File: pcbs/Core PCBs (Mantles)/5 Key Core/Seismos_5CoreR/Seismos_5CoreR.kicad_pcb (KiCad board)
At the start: 2 copper layers, 147 x 78 mm, 27 parts, among them J1 SM09B-SRSS-TB(LF)(SN), J2 SM09B-SRSS-TB(LF)(SN), J3 SM09B-SRSS-TB(LF)(SN), J4 SM09B-SRSS-TB(LF)(SN), J5 SM09B-SRSS-TB(LF)(SN), J6 SM09B-SRSS-TB(LF)(SN), J7 SM09B-SRSS-TB(LF)(SN), J8 MJ-4PP-9-Lily58, J9 Conn_01x05_Pin, SW1 RotaryEncoder_Switch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

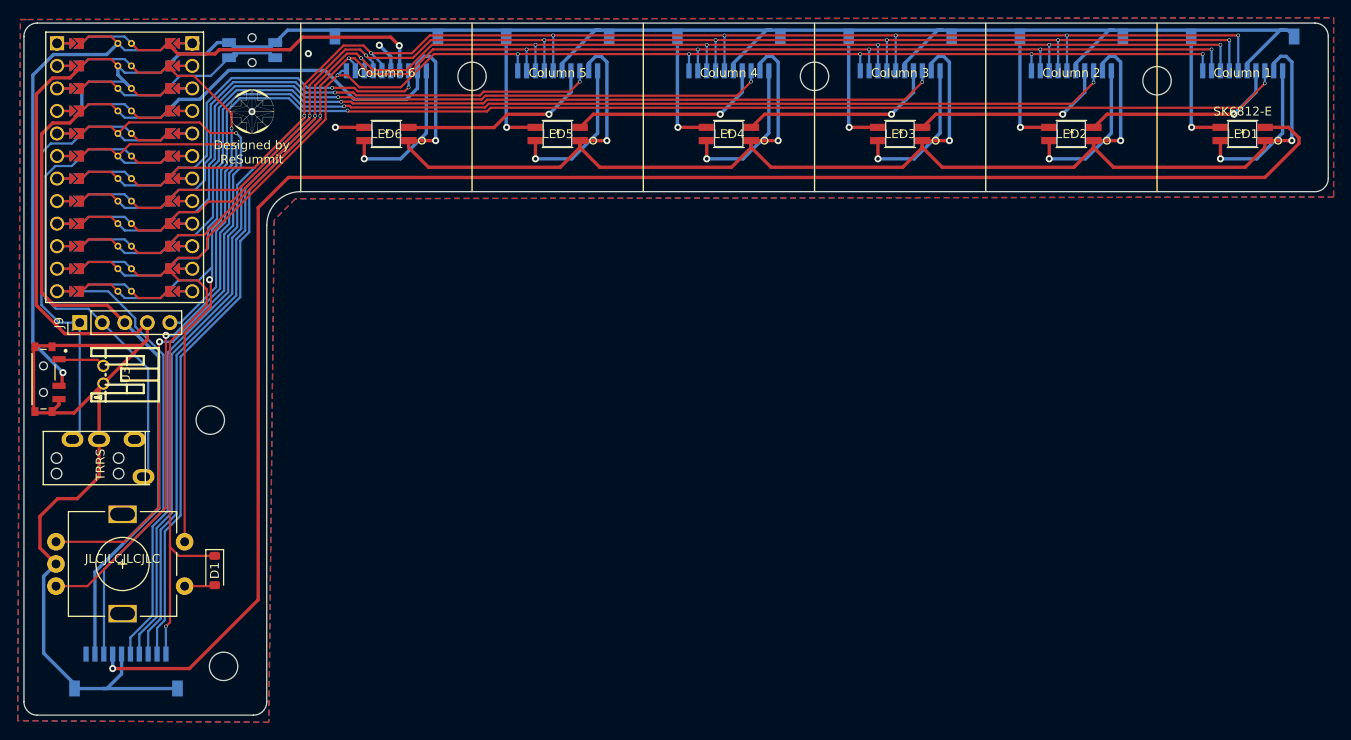
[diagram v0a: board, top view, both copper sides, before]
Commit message: Release v1.1
***NOTE***: If you have a previous commit, please update your files.
This commit fixes the incorrect RGB pinout and power switch as the
RGB footprint was incorrect.
The power switch behaviour is also fixed in this commit so the position
matches on both sides.
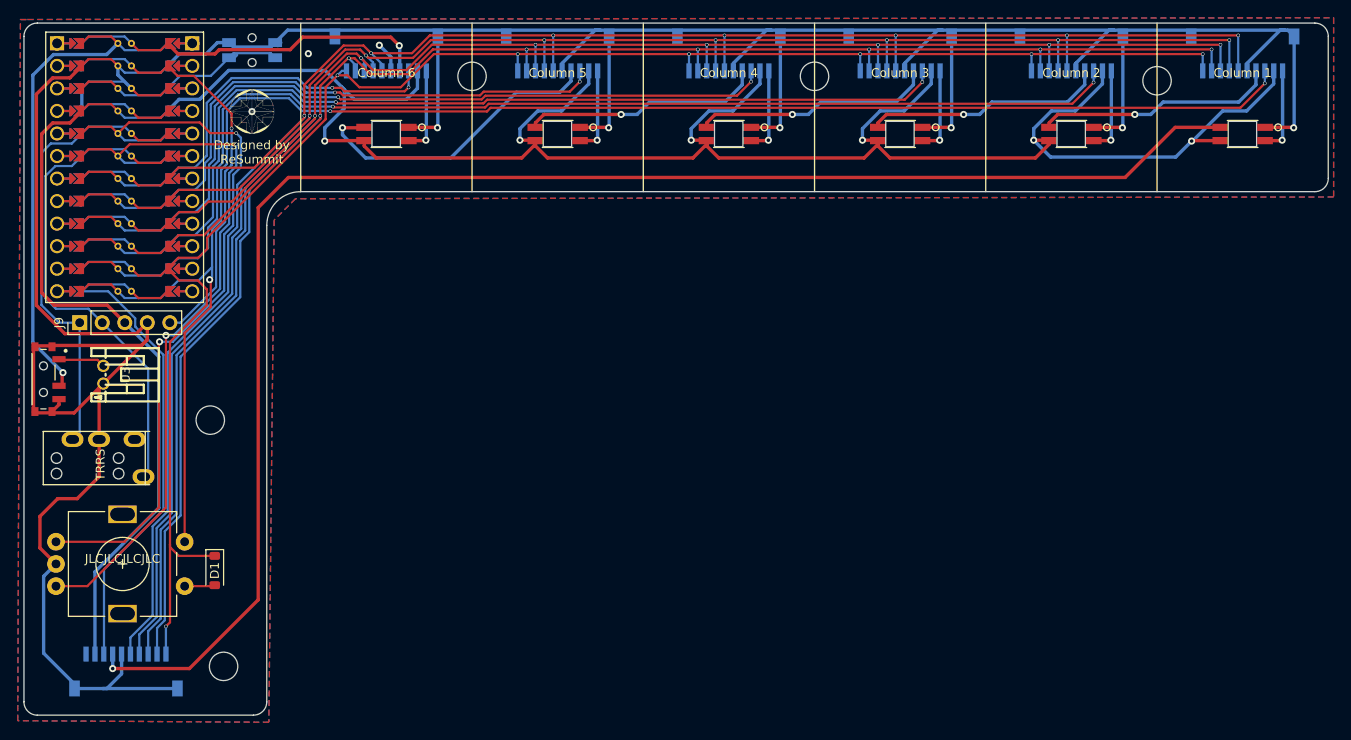
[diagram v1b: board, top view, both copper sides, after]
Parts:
- LED1, LED2, LED3, LED4, LED5, LED6: moved to F.Cu
- turned LED1 to 180 degrees
- turned LED2 to 180 degrees
- turned LED3 to 180 degrees
- turned LED4 to 180 degrees
- turned LED5 to 180 degrees
- turned LED6 to 180 degrees
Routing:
- net /V+: track 315.9 -> 301.2 mm
- net /RGB_In7: track 190.7 -> 177.6 mm
- net /RGB_In2: track 22.3 -> 34.8 mm
- net GND: track 385.6 -> 396.2 mm
- net /RGB_Out6: track 17.3 -> 9.80 mm
- net /RGB_Out4: track 17.3 -> 9.80 mm
- net /RGB_Out1: track 17.3 -> 9.80 mm
- net /RGB_Out3: track 17.3 -> 9.80 mm
- net /RGB_Out2: track 17.3 -> 9.80 mm
- net /RGB_Out5: track 17.3 -> 9.80 mm
- net /RGB_In4: track 22.3 -> 27.1 mm
- net /RGB_In6: track 22.3 -> 27.1 mm
- net /RGB_In3: track 22.3 -> 27.1 mm
- net /RGB_In5: track 22.3 -> 27.1 mm
- net SDA: track 42.4 -> 41.2 mm
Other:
- board text added: "Rev. 1.1"
- board text removed: "Rev. 1.0"

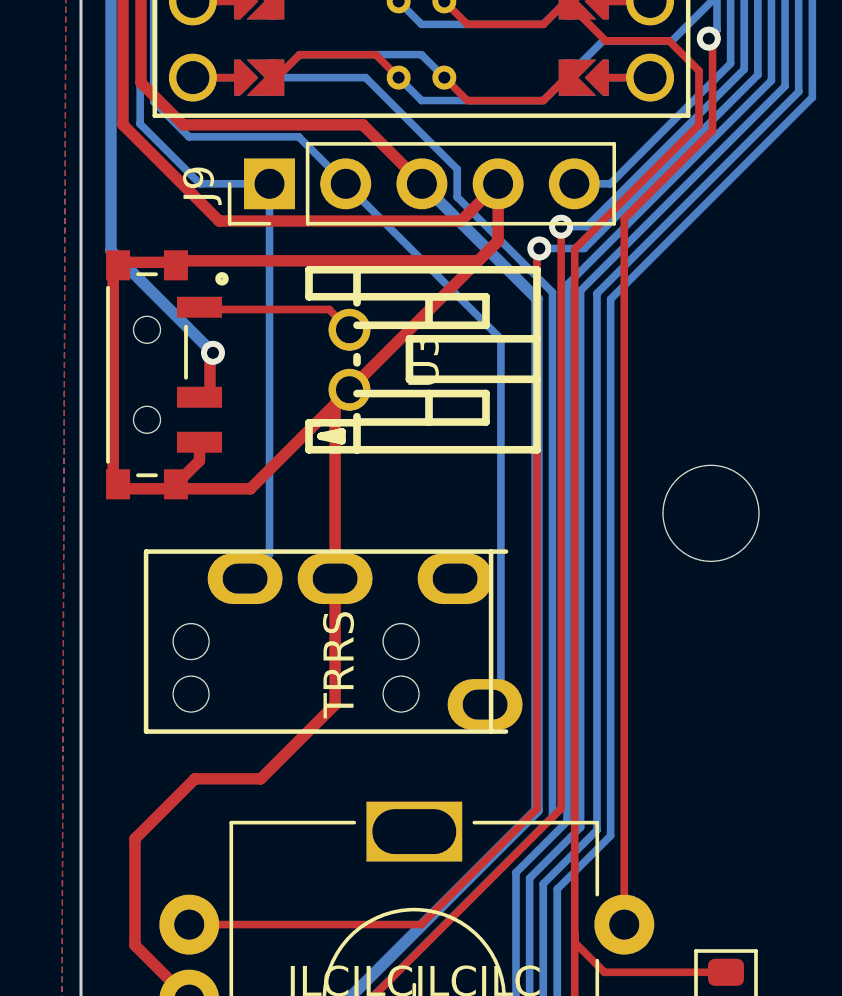
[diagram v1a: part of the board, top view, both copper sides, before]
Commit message: Release v1.1.1
Added I2C pull up resistors and bridge contacts on the backif 5V power
is desired. If you have v1.1, V+ is actually close to the headphone
jack, so you can scratch off the trace and bridge there.
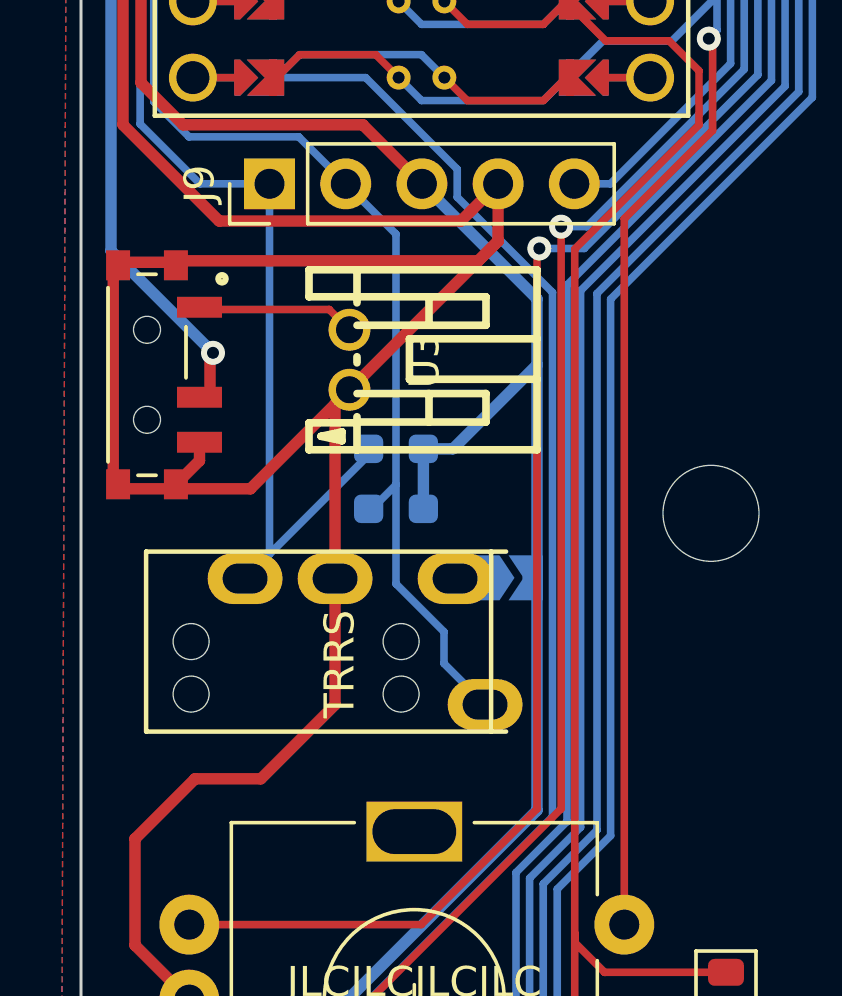
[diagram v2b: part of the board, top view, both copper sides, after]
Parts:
- added JP1: Jumper_2_Open, Jumper:SolderJumper-2_P1.3mm_Open_TrianglePad1.0x1.5mm, B.Cu at (44.2, 66.9)
- added R1: R, Resistor_SMD:R_0603_1608Metric_Pad0.98x0.95mm_HandSolder, B.Cu at (40.5, 62.6)
- added R2: R, Resistor_SMD:R_0603_1608Metric_Pad0.98x0.95mm_HandSolder, B.Cu at (40.5, 64.6)
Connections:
- J8 pad 1: unconnected-(J8-Pad1) -> Net-(JP1-A)
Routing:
- net /V+: track 301.2 -> 308.4 mm
- net SDA: track 41.2 -> 47.3 mm
- net SCL: track 46.1 -> 46.9 mm
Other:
- board text added: "Rev. 1.1.1"
- board text removed: "Rev. 1.1"
